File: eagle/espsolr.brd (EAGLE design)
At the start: 75.9 x 50.8 mm, 22 parts, among them IC1 ATtiny85

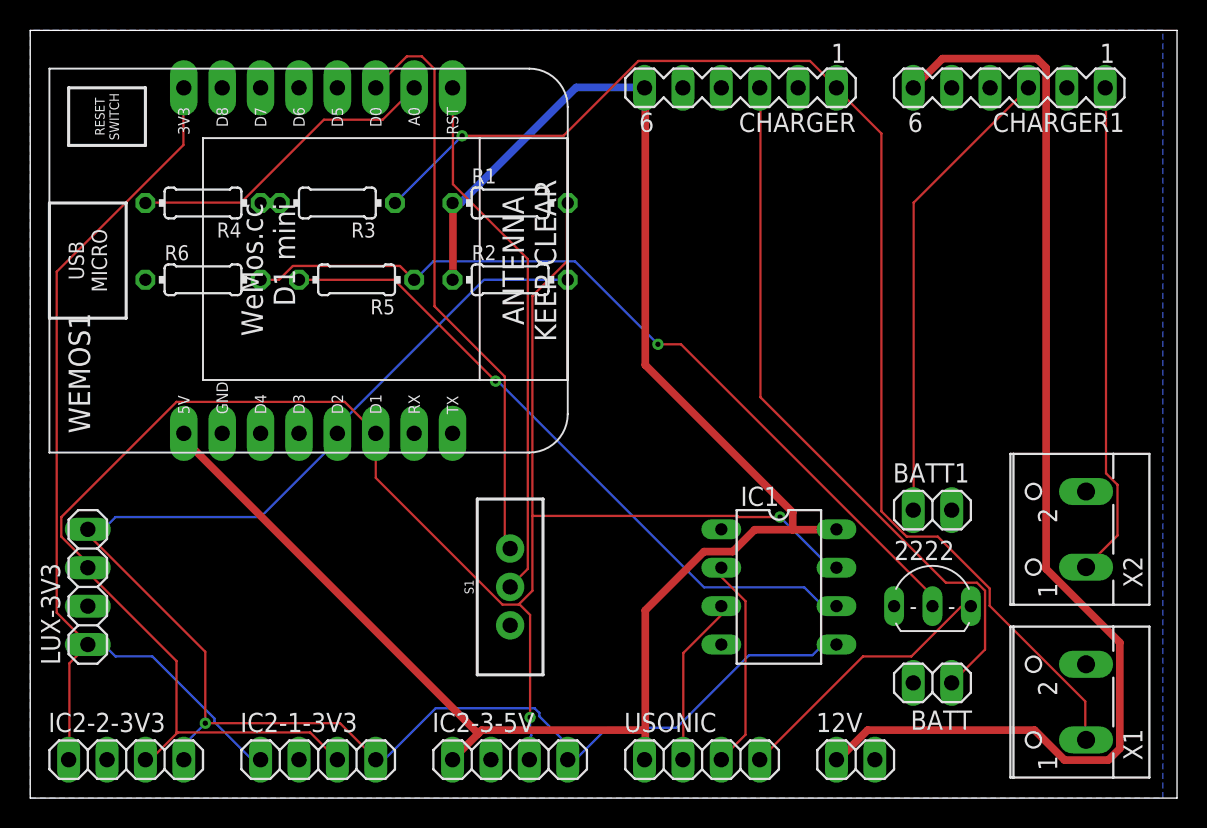
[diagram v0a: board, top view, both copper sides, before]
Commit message: removed the 12v i2c from the board - what was i thinking?
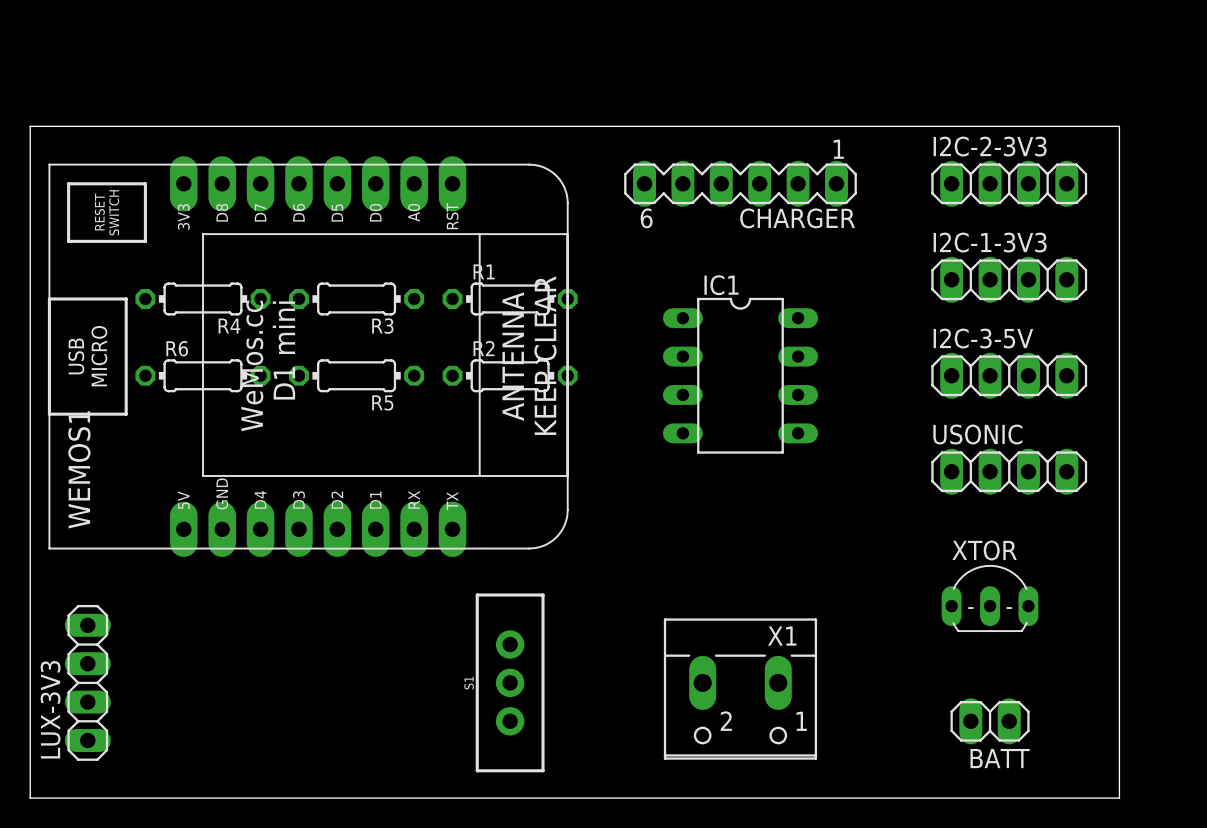
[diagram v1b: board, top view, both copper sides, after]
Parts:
- removed 12V, BATT1: (no value), pinhead:1X02
- removed 2222: (no value), transistor-neu-to92:TO92-EBC
- removed CHARGER1: 12v, con-lstb:MA06-1
- removed IC2-1-3V3, IC2-2-3V3, IC2-3-5V: (no value), pinhead:1X04
- removed X2: (no value), con-wago-500:W237-102
- added I2C-1-3V3, I2C-2-3V3, I2C-3-5V: (no value), pinhead:1X04
- added XTOR: 2222, transistor-neu-to92:TO92-EBC
- BATT: value (none) -> 3v7
- moved USONIC 27.9 mm to (64.8, 21.6)
- moved X1 21.6 mm to (47.0, 6.35), turned to 180 degrees
- moved IC1 14.2 mm to (47.0, 27.9)
- moved R3 6.48 mm to (21.6, 33.0)
- moved CHARGER 6.35 mm to (47.0, 40.6)
- moved LUX-3V3 6.35 mm to (3.81, 7.62)
- moved S1 6.35 mm to (31.8, 7.62)
- moved R2 6.35 mm to (31.8, 27.9)
- moved R5 6.35 mm to (21.6, 27.9)
- moved R6 6.35 mm to (11.4, 27.9)
- moved WEMOS1 6.35 mm to (20.3, 30.5)
- moved R1 6.35 mm to (31.8, 33.0)
- moved R4 6.35 mm to (11.4, 33.0)
- moved BATT 4.58 mm to (63.5, 5.08)
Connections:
- removed net +12V: 12V.1, CHARGER1.6
- removed net BAT12+: BATT1.1, CHARGER1.3
- removed net SOLAR12+: CHARGER1.1, X2.1
- net +3V3: now also I2C-1-3V3.1, I2C-2-3V3.1; no longer IC2-1-3V3.1, IC2-2-3V3.1
- net +5V: now also I2C-3-5V.1; no longer IC2-3-5V.1
- net GND: now also I2C-1-3V3.2, I2C-2-3V3.2, I2C-3-5V.2, XTOR.E; no longer 12V.2, 2222.E, BATT1.2, CHARGER1.2, CHARGER1.4, CHARGER1.5, IC2-1-3V3.2, IC2-2-3V3.2, IC2-3-5V.2, X2.2
- net N$10: now also XTOR.B; no longer 2222.B
- net N$9: now also XTOR.C; no longer 2222.C
- net SCL: now also I2C-1-3V3.3, I2C-2-3V3.3, I2C-3-5V.3; no longer IC2-1-3V3.3, IC2-2-3V3.3, IC2-3-5V.3
- net SDA: now also I2C-1-3V3.4, I2C-2-3V3.4, I2C-3-5V.4; no longer IC2-1-3V3.4, IC2-2-3V3.4, IC2-3-5V.4
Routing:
- net SCL: track 132.5 -> 0.00 mm, vias 2 -> 0
- net +5V: track 120.6 -> 0.00 mm
- net SDA: track 107.7 -> 0.00 mm, vias 1 -> 0
- net SOLAR+: track 85.0 -> 0.00 mm, vias 1 -> 0
- net +12V: track 77.6 -> 0.00 mm
- net +3V3: track 64.1 -> 0.00 mm
- net N$10: track 55.6 -> 0.00 mm, vias 1 -> 0
- net BAT+: track 47.7 -> 0.00 mm
- net NPN: track 44.5 -> 0.00 mm, vias 1 -> 0
- net D0: track 38.9 -> 0.00 mm
- net RESET: track 35.6 -> 0.00 mm
- net SOLAR12+: track 32.9 -> 0.00 mm
- net BAT12+: track 31.1 -> 0.00 mm
- net N$2: track 21.0 -> 0.00 mm
- net N$9: track 18.2 -> 0.00 mm
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- removed copper zone on layer 16, net GND
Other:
- board size 75.9 x 50.8 mm -> 72.1 x 44.4 mm

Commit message: updated board and created gerbers
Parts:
- removed R6: 120k, resistor:0204/7
- R5: value 120k -> 270
- turned LUX-3V3 to 270 degrees
- renumbered X1 to SOLAR
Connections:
- net GND: no longer R6.1
- net N$10: no longer R6.2
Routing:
- net SCL: track 0.00 -> 109.2 mm
- net SDA: track 0.00 -> 96.9 mm
- net +3V3: track 0.00 -> 92.6 mm, vias 0 -> 1
- net SOLAR+: track 0.00 -> 85.3 mm
- net +5V: track 0.00 -> 76.3 mm
- net RESET: track 0.00 -> 45.1 mm
- net N$10: track 0.00 -> 44.4 mm, vias 0 -> 1
- net BAT+: track 0.00 -> 43.8 mm
- net D0: track 0.00 -> 42.2 mm
- net NPN: track 0.00 -> 34.3 mm
- net N$7: track 0.00 -> 26.3 mm, vias 0 -> 1
- net N$8: track 0.00 -> 22.4 mm
- net N$2: track 0.00 -> 21.0 mm
- net N$9: track 0.00 -> 9.94 mm
- net N$1: track 0.00 -> 2.58 mm
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- added copper zone on layer 16, net GND
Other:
- board size 72.1 x 44.4 mm -> 70.8 x 44.4 mm
- board text added: "BJF 2018 Tank Sensor v1"
- board text added: "Gnd"
- board text added: "Run"
- board text added: "SCL"
- board text added: "SDA"
- board text added: "Sleep"
- board text added: "VCC"
- board text added: "Vcc"
- board text added: "Vin"
- board text added: "pb3"
- board text added: "pb4"

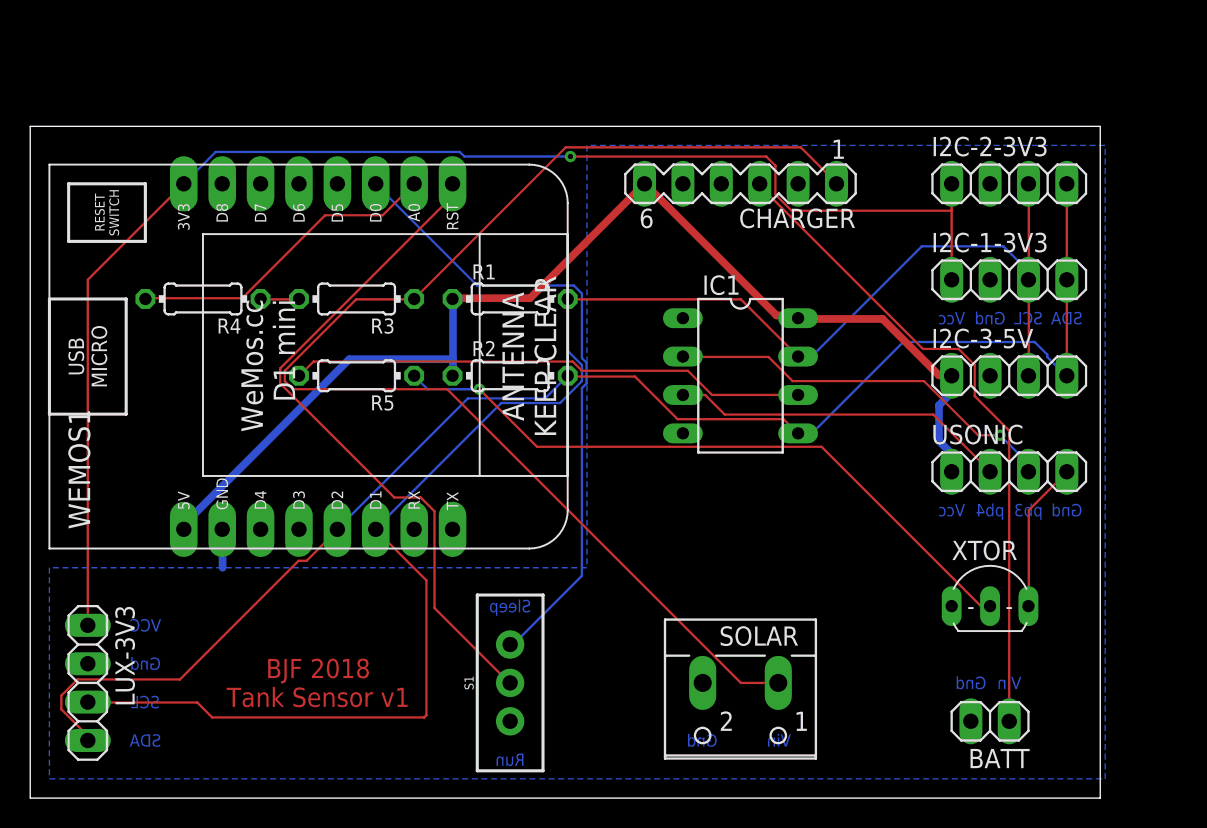
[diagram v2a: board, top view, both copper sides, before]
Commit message: fixed the analog pin to battery - duh!
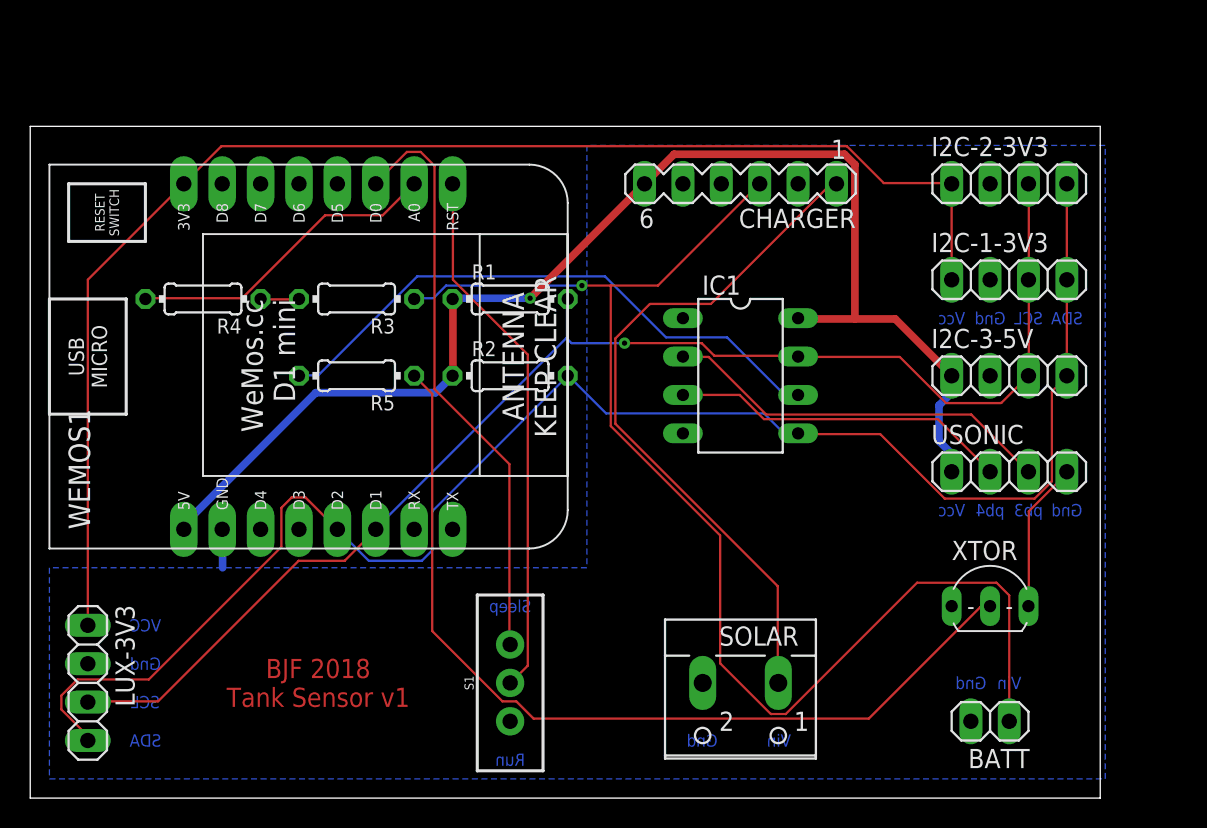
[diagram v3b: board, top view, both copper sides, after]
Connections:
- net BAT+: now also R3.1
- net SOLAR+: no longer R3.1
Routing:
- net BAT+: track 43.8 -> 86.8 mm, vias 0 -> 1
- net SOLAR+: track 85.3 -> 46.2 mm
- net SCL: track 109.2 -> 90.2 mm, vias 0 -> 1
- net N$10: track 44.4 -> 59.8 mm, vias 1 -> 0
- net SDA: track 96.9 -> 108.5 mm
- net +5V: track 76.3 -> 87.2 mm, vias 0 -> 1
- net RESET: track 45.1 -> 35.6 mm
- net NPN: track 34.3 -> 39.0 mm
- net D0: track 42.2 -> 38.9 mm
- net +3V3: track 92.6 -> 91.1 mm, vias 1 -> 0
- net N$7: track 26.3 -> 26.0 mm, vias 1 -> 0

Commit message: tweaked size and layers
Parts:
- moved I2C-2-3V3 22.2 mm to (53.3, 21.6)
- moved XTOR 22.2 mm to (41.9, 19.1)
- moved BATT 21.6 mm to (41.9, 5.08)
- moved I2C-1-3V3 21.1 mm to (53.3, 16.5)
- moved I2C-3-5V 21.1 mm to (53.3, 10.2)
- moved USONIC 20.1 mm to (53.3, 5.08)
- moved SOLAR 15.3 mm to (31.8, 7.62), turned to 0 degrees
- moved S1 10.2 mm to (21.6, 7.62)
- moved IC1 2.54 mm to (47.0, 30.5)
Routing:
- net SDA: track 108.5 -> 0.00 mm
- net +3V3: track 91.1 -> 0.00 mm
- net SCL: track 90.2 -> 0.00 mm, vias 1 -> 0
- net +5V: track 87.2 -> 0.00 mm, vias 1 -> 0
- net BAT+: track 86.8 -> 0.00 mm, vias 1 -> 0
- net N$10: track 59.8 -> 0.00 mm
- net SOLAR+: track 46.2 -> 0.00 mm
- net NPN: track 39.0 -> 0.00 mm
- net D0: track 38.9 -> 0.00 mm
- net RESET: track 35.6 -> 0.00 mm
- net N$7: track 26.0 -> 0.00 mm
- net N$8: track 22.4 -> 0.00 mm
- net N$2: track 21.0 -> 0.00 mm
- net N$9: track 9.94 -> 0.00 mm
- net N$1: track 2.58 -> 0.00 mm
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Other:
- board size 70.8 x 44.4 mm -> 59.4 x 44.4 mm
- board text added: "BJF 2018 Tank Sensor v1.1"
- board text removed: "BJF 2018 Tank Sensor v1"
